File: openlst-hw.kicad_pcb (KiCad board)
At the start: 4 copper layers, 60 x 50 mm, 175 parts, among them J1 5VDC, J2 CC Prog/Debug, J3 UART0, J4 UART1, J5 Control Outputs, J6 ANT, U1 LM1117-3.3, U2 CC1110, U3 LT1086-3.6, U4 FOX924 27MHz, U5 TLV803S, U6 PE4259, U8 STA1120A, U9 RFFM6403

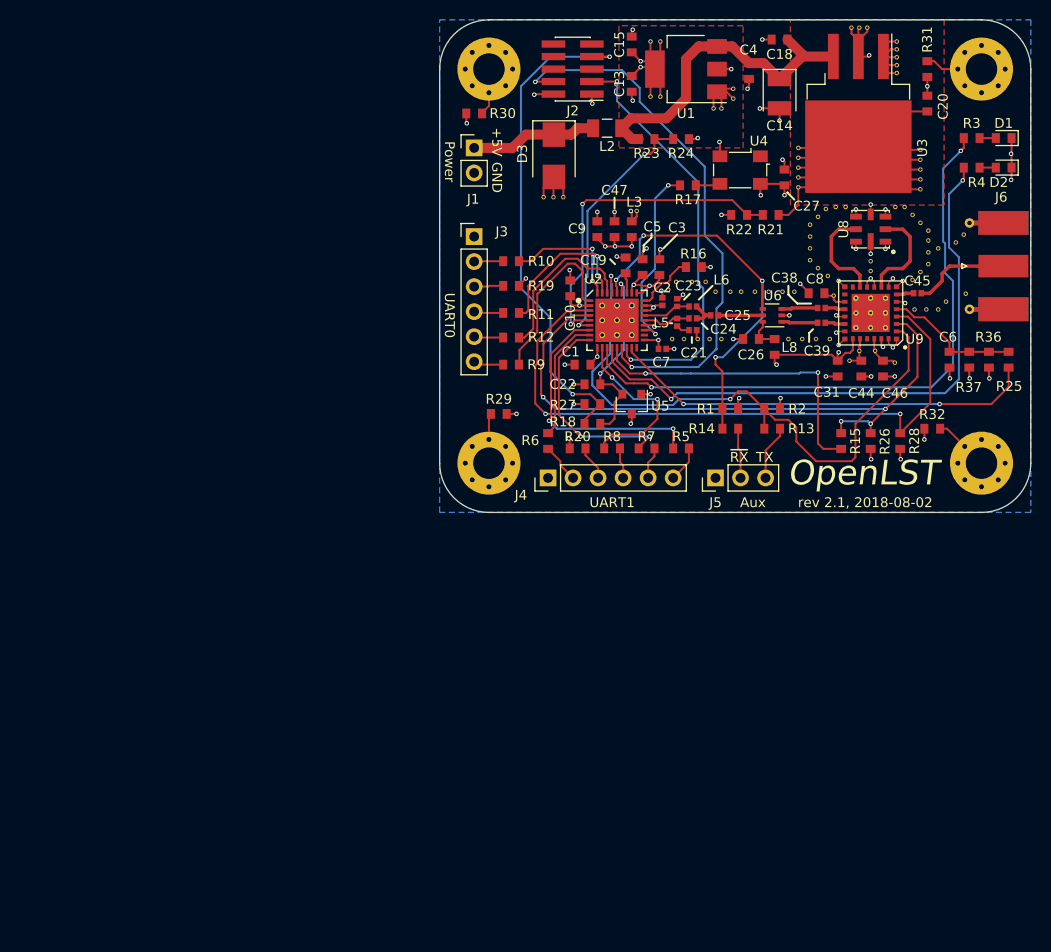
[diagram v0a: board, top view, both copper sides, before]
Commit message: Radio board done, except for artwork touchup
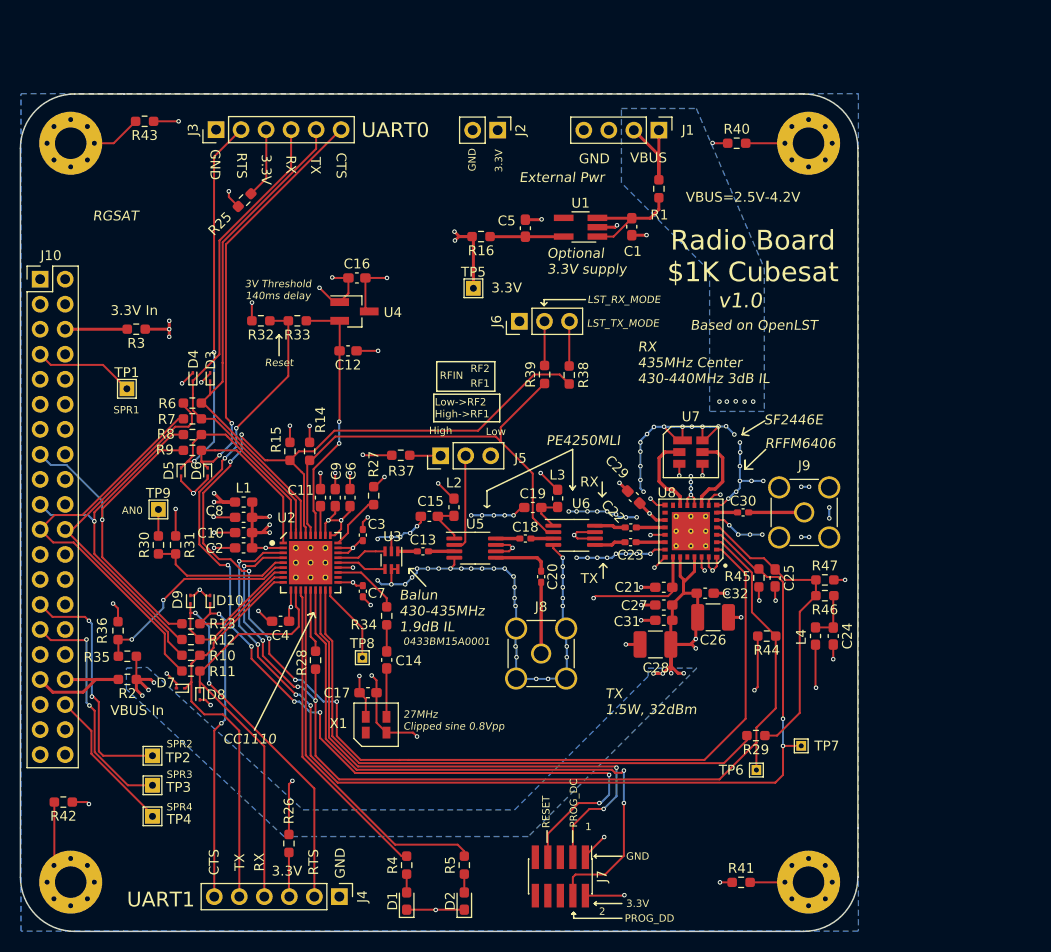
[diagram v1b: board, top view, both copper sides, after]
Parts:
- removed C38, C39, C45: 220p, archive:C_0402_1005Metric
- removed C44, C46, C47: 1u, archive:C_0603_1608Metric
- removed L5, L6: 27n, archive:L_0402_1005Metric
- removed L8: Z=1k @ 100M, archive:L_0603_1608Metric
- removed MK1, MK2, MK3, MK4: M3_Hole, archive:MountingHole_3.2mm_M3_Pad_Via
- removed R17: 100, archive:R_0603_1608Metric
- removed R18: 1K, archive:R_0603_1608Metric
- removed R19, R20: DNI, archive:R_0603_1608Metric
- removed R21, R23: 33K, archive:R_0603_1608Metric
- removed R22, R24: 10K, archive:R_0603_1608Metric
- removed REF** (x85): VIA-10mil, openlst:VIA-10mil
- removed U9: RFFM6403, openlst:Qorvo_LGA_28_ThermalVias
- added C11: 1uF, Capacitor_SMD:C_0603_1608Metric_Pad1.08x0.95mm_HandSolder, F.Cu at (101.4, 87.0)
- added C12: 0.01uF, Capacitor_SMD:C_0603_1608Metric_Pad1.08x0.95mm_HandSolder, F.Cu at (104.2, 72.1)
- added C16: 0.1uF, Capacitor_SMD:C_0603_1608Metric_Pad1.08x0.95mm_HandSolder, F.Cu at (105.1, 64.7)
- added C17: 0.1uF, Capacitor_SMD:C_0603_1608Metric_Pad1.08x0.95mm_HandSolder, F.Cu at (106.2, 106.8)
- added C28: 47uF, Capacitor_SMD:C_1210_3225Metric_Pad1.33x2.70mm_HandSolder, F.Cu at (135.4, 101.9)
- added C29: 0.1uF, Capacitor_SMD:C_0603_1608Metric_Pad1.08x0.95mm_HandSolder, F.Cu at (133.2, 87.0)
- added C30: 220pF, Capacitor_SMD:C_0402_1005Metric_Pad0.74x0.62mm_HandSolder, F.Cu at (144.3, 88.5)
- added C32: 0.1uF, Capacitor_SMD:C_0603_1608Metric_Pad1.08x0.95mm_HandSolder, F.Cu at (140.4, 96.7)
- added D10: ESD9B5.0ST5G, Diode_SMD:D_SOD-923, F.Cu at (90.2, 97.3)
- added D4: ESD9B5.0ST5G, Diode_SMD:D_SOD-923, F.Cu at (88.5, 74.8)
- added D5: ESD9B5.0ST5G, Diode_SMD:D_SOD-923, F.Cu at (87.2, 84.4)
- added D6: ESD9B5.0ST5G, Diode_SMD:D_SOD-923, F.Cu at (90.0, 84.4)
- added D7: ESD9B5.0ST5G, Diode_SMD:D_SOD-923, F.Cu at (87.2, 106.3)
- added D8: ESD9B5.0ST5G, Diode_SMD:D_SOD-923, F.Cu at (89.2, 107.1)
- added D9: ESD9B5.0ST5G, Diode_SMD:D_SOD-923, F.Cu at (88.2, 97.3)
- added H1: MountingHole_Pad, MountingHole:MountingHole_3.2mm_M3_Pad_Via, F.Cu at (150.9, 51.0)
- added H2: MountingHole_Pad, MountingHole:MountingHole_3.2mm_M3_Pad_Via, F.Cu at (150.9, 126.0)
- added H3: MountingHole_Pad, MountingHole:MountingHole_3.2mm_M3_Pad_Via, F.Cu at (76.0, 126.0)
- added H4: MountingHole_Pad, MountingHole:MountingHole_3.2mm_M3_Pad_Via, F.Cu at (76.0, 51.0)
- added J10: Conn_02x20_Odd_Even, Connector_PinHeader_2.54mm:PinHeader_2x20_P2.54mm_Vertical, F.Cu at (72.9, 64.8)
- added J7: CC Prog/Debug, Connector_PinHeader_1.27mm:PinHeader_2x05_P1.27mm_Vertical_SMD, F.Cu at (125.8, 125.5)
- added J8: Conn_Coaxial, Connector_Coaxial:SMA_Amphenol_901-144_Vertical, F.Cu at (123.8, 102.8)
- added J9: ANT, Connector_Coaxial:SMA_Amphenol_901-144_Vertical, F.Cu at (150.5, 88.5)
- added L1: Z=1k @ 100M, Inductor_SMD:L_0603_1608Metric_Pad1.05x0.95mm_HandSolder, F.Cu at (93.6, 87.5)
- added L4: Z=1k @ 100M, Inductor_SMD:L_0603_1608Metric_Pad1.05x0.95mm_HandSolder, F.Cu at (151.7, 101.0)
- added R33: 1K, Resistor_SMD:R_0603_1608Metric_Pad0.98x0.95mm_HandSolder, F.Cu at (99.0, 69.0)
- added R34: 0, Resistor_SMD:R_0603_1608Metric_Pad0.98x0.95mm_HandSolder, F.Cu at (108.1, 99.0)
- added R35: 20K, Resistor_SMD:R_0603_1608Metric_Pad0.98x0.95mm_HandSolder, F.Cu at (81.8, 103.1)
- added R38: 100, Resistor_SMD:R_0603_1608Metric_Pad0.98x0.95mm_HandSolder, F.Cu at (126.7, 74.5)
- added R39: 100, Resistor_SMD:R_0603_1608Metric_Pad0.98x0.95mm_HandSolder, F.Cu at (124.2, 74.5)
- added R40: DNP, Resistor_SMD:R_0603_1608Metric_Pad0.98x0.95mm_HandSolder, F.Cu at (143.7, 51.0)
- added R41: DNP, Resistor_SMD:R_0603_1608Metric_Pad0.98x0.95mm_HandSolder, F.Cu at (144.1, 126.0)
- added R42: DNP, Resistor_SMD:R_0603_1608Metric_Pad0.98x0.95mm_HandSolder, F.Cu at (75.3, 117.9)
- added R43: DNP, Resistor_SMD:R_0603_1608Metric_Pad0.98x0.95mm_HandSolder, F.Cu at (83.5, 48.8)
- added R44: 1K, Resistor_SMD:R_0603_1608Metric_Pad0.98x0.95mm_HandSolder, F.Cu at (146.7, 101.0)
- added R45: 1K, Resistor_SMD:R_0603_1608Metric_Pad0.98x0.95mm_HandSolder, F.Cu at (145.9, 95.2)
- added R46: 3.09K, Resistor_SMD:R_0603_1608Metric_Pad0.98x0.95mm_HandSolder, F.Cu at (152.6, 97.0)
- added R47: 6.65K, Resistor_SMD:R_0603_1608Metric_Pad0.98x0.95mm_HandSolder, F.Cu at (152.6, 95.3)
- added TP1: TP_1.5x1.5, TestPoint:TestPoint_THTPad_1.5x1.5mm_Drill0.7mm, F.Cu at (81.8, 76.0)
- added TP2: TP_1.5x1.5, TestPoint:TestPoint_THTPad_1.5x1.5mm_Drill0.7mm, F.Cu at (84.3, 113.2)
- added TP3: TP_1.5x1.5, TestPoint:TestPoint_THTPad_1.5x1.5mm_Drill0.7mm, F.Cu at (84.3, 116.2)
- added TP4: TP_1.5x1.5, TestPoint:TestPoint_THTPad_1.5x1.5mm_Drill0.7mm, F.Cu at (84.3, 119.3)
- added TP5: TP_1.5x1.5, TestPoint:TestPoint_THTPad_1.5x1.5mm_Drill0.7mm, F.Cu at (116.9, 65.8)
- added TP6: TP_tht_1x1, TestPoint:TestPoint_THTPad_1.0x1.0mm_Drill0.5mm, F.Cu at (145.7, 114.7)
- added TP7: TP_tht_1x1, TestPoint:TestPoint_THTPad_1.0x1.0mm_Drill0.5mm, F.Cu at (150.2, 112.2)
- added TP8: TP_tht_1x1, TestPoint:TestPoint_THTPad_1.0x1.0mm_Drill0.5mm, F.Cu at (105.7, 103.2)
- added TP9: TP_1.5x1.5, TestPoint:TestPoint_THTPad_1.5x1.5mm_Drill0.7mm, F.Cu at (85.0, 88.2)
- added U7: SF2446E, footprint_custom:SF2446E, F.Cu at (139.0, 82.4)
- added X1: TG2520SMN 27MHz, footprint_custom:TG2520SMN, F.Cu at (107.0, 110.0)
- C1, C31, C5: value 0.1u -> 4.7uF; footprint archive:C_0603_1608Metric -> Capacitor_SMD:C_0603_1608Metric_Pad1.08x0.95mm_HandSolder
- C10, C27, C8: value 0.1u -> 1uF; footprint archive:C_0603_1608Metric -> Capacitor_SMD:C_0603_1608Metric_Pad1.08x0.95mm_HandSolder
- C13, C18, C20: value 10u -> 220pF; footprint archive:C_0603_1608Metric -> Capacitor_SMD:C_0402_1005Metric_Pad0.74x0.62mm_HandSolder
- C14: value 100u -> 0.01uF; footprint archive:CP_EIA-3528-15_AVX-H -> Capacitor_SMD:C_0603_1608Metric_Pad1.08x0.95mm_HandSolder
- C15, C6: value 0.1u -> 0.1uF; footprint archive:C_0603_1608Metric -> Capacitor_SMD:C_0603_1608Metric_Pad1.08x0.95mm_HandSolder
- C19: value 1n -> 0.1uF; footprint archive:C_0603_1608Metric -> Capacitor_SMD:C_0603_1608Metric_Pad1.08x0.95mm_HandSolder
- C2, C21, C25: value 220p -> 0.1uF; footprint archive:C_0402_1005Metric -> Capacitor_SMD:C_0603_1608Metric_Pad1.08x0.95mm_HandSolder
- C22: value 1n -> 220pF; footprint archive:C_0603_1608Metric -> Capacitor_SMD:C_0402_1005Metric_Pad0.74x0.62mm_HandSolder
- C23: value 3.9p -> 220pF; footprint archive:C_0402_1005Metric -> Capacitor_SMD:C_0402_1005Metric_Pad0.74x0.62mm_HandSolder
- C24: value 3.9p -> 0.1uF; footprint archive:C_0402_1005Metric -> Capacitor_SMD:C_0603_1608Metric_Pad1.08x0.95mm_HandSolder
- C26: value 0.1u -> 47uF; footprint archive:C_0603_1608Metric -> Capacitor_SMD:C_1210_3225Metric_Pad1.33x2.70mm_HandSolder
- C3: value 0.1u -> 220pF; footprint archive:C_0603_1608Metric -> Capacitor_SMD:C_0402_1005Metric_Pad0.74x0.62mm_HandSolder
- C4: value 10u -> 0.1uF; footprint archive:C_0603_1608Metric -> Capacitor_SMD:C_0603_1608Metric_Pad1.08x0.95mm_HandSolder
- C7: value 220p -> 220pF; footprint archive:C_0402_1005Metric -> Capacitor_SMD:C_0402_1005Metric_Pad0.74x0.62mm_HandSolder
- C9: value 1u -> 0.1uF; footprint archive:C_0603_1608Metric -> Capacitor_SMD:C_0603_1608Metric_Pad1.08x0.95mm_HandSolder
- D1, D2: value LED -> LED_SMD_RED; footprint archive:LED_0603_1608Metric -> LED_SMD:LED_0603_1608Metric_Pad1.05x0.95mm_HandSolder
- D3: value STPS340U -> ESD9B5.0ST5G; footprint archive:D_SMB -> Diode_SMD:D_SOD-923
- J1: value 5VDC -> EXT VBUS; footprint archive:PinHeader_1x02_P2.54mm_Vertical -> Connector_PinHeader_2.54mm:PinHeader_1x04_P2.54mm_Vertical
- J2: value CC Prog/Debug -> EXT 3.3V; footprint archive:PinHeader_2x05_P1.27mm_Vertical_SMD -> Connector_PinHeader_2.54mm:PinHeader_1x02_P2.54mm_Vertical
- J3, J4: footprint archive:PinHeader_1x06_P2.54mm_Vertical -> Connector_PinHeader_2.54mm:PinHeader_1x06_P2.54mm_Vertical
- J5: value Control Outputs -> Switch Select; footprint archive:PinHeader_1x03_P2.54mm_Vertical -> Connector_PinHeader_2.54mm:PinHeader_1x03_P2.54mm_Vertical
- J6: value ANT -> Control Outputs; footprint archive:SMA_Molex_73251-1153_EdgeMount_Horizontal -> Connector_PinHeader_2.54mm:PinHeader_1x03_P2.54mm_Vertical
- L2: value Z=500 @ 100M -> Z=1k @ 100M; footprint archive:L_1206_3216Metric -> Inductor_SMD:L_0603_1608Metric_Pad1.05x0.95mm_HandSolder
- L3: footprint archive:L_0603_1608Metric -> Inductor_SMD:L_0603_1608Metric_Pad1.05x0.95mm_HandSolder
- R1, R26, R28: value 1K -> DNP; footprint archive:R_0603_1608Metric -> Resistor_SMD:R_0603_1608Metric_Pad0.98x0.95mm_HandSolder
- R10, R11, R12, R13: value 100 -> DNP; footprint archive:R_0603_1608Metric -> Resistor_SMD:R_0603_1608Metric_Pad0.98x0.95mm_HandSolder
- R14, R5: value 100 -> 1K; footprint archive:R_0603_1608Metric -> Resistor_SMD:R_0603_1608Metric_Pad0.98x0.95mm_HandSolder
- R15: value DNI -> 1K; footprint archive:R_0603_1608Metric -> Resistor_SMD:R_0603_1608Metric_Pad0.98x0.95mm_HandSolder
- R16: value 56K -> 0; footprint archive:R_0603_1608Metric -> Resistor_SMD:R_0603_1608Metric_Pad0.98x0.95mm_HandSolder
- R2, R3: value 1K -> 10m; footprint archive:R_0603_1608Metric -> Resistor_SMD:R_0603_1608Metric_Pad0.98x0.95mm_HandSolder
- R25, R29, R30, R31: value DNI -> DNP; footprint archive:R_0603_1608Metric -> Resistor_SMD:R_0603_1608Metric_Pad0.98x0.95mm_HandSolder
- R27: value 33K -> 56K; footprint archive:R_0603_1608Metric -> Resistor_SMD:R_0603_1608Metric_Pad0.98x0.95mm_HandSolder
- R32: value DNI -> 47K; footprint archive:R_0603_1608Metric -> Resistor_SMD:R_0603_1608Metric_Pad0.98x0.95mm_HandSolder
- R36: value 5K6 -> 47K; footprint archive:R_0603_1608Metric -> Resistor_SMD:R_0603_1608Metric_Pad0.98x0.95mm_HandSolder
- R37: value 3K3 -> 1K; footprint archive:R_0603_1608Metric -> Resistor_SMD:R_0603_1608Metric_Pad0.98x0.95mm_HandSolder
- R4, R6, R7, R8, R9: footprint archive:R_0603_1608Metric -> Resistor_SMD:R_0603_1608Metric_Pad0.98x0.95mm_HandSolder
- U1: value LM1117-3.3 -> ADP150AUJZ-3.3-R7; footprint archive:SOT-223-3_TabPin2 -> Package_TO_SOT_SMD:TSOT-23-5_HandSoldering
- U3: value LT1086-3.6 -> 0433BM15A0001; footprint archive:TO-263-3_TabPin2 -> RF_Converter:Balun_Johanson_0896BM15A0001
- U4: value FOX924 27MHz -> MIC803; footprint archive:Oscillator_SMD_Fordahl_DFAS15-4Pin_5.0x3.2mm -> Package_TO_SOT_SMD:SOT-23_Handsoldering
- U5: value TLV803S -> PE4250MLI; footprint archive:SOT-23 -> Package_SO:MSOP-8_3x3mm_P0.65mm
- U6: value PE4259 -> PE4250MLI; footprint archive:SOT-363_SC-70-6 -> Package_SO:MSOP-8_3x3mm_P0.65mm
- U8: value STA1120A -> RFFM6406; footprint openlst:SAW-8_3.8mm -> openlst:Qorvo_LGA_28_ThermalVias
- moved D1 98.3 mm to (110.2, 128.0), turned to 90 degrees
- moved R36 92.6 mm to (80.8, 100.5)
- moved D2 92.4 mm to (116.0, 128.0), turned to 90 degrees
- moved R4 91.1 mm to (110.2, 124.3), turned to 90 degrees
- moved R31 90.3 mm to (86.7, 91.8), turned to 270 degrees
- moved R3 87.0 mm to (82.7, 69.9)
- moved R25 79.2 mm to (93.7, 56.8), turned to 225 degrees
- moved C4 73.4 mm to (97.3, 99.5), turned to 180 degrees
- moved R26 71.8 mm to (98.2, 122.1)
- moved R2 71.0 mm to (81.8, 105.5)
- moved C14 70.0 mm to (108.1, 103.5), turned to 90 degrees
- moved R32 69.0 mm to (95.3, 69.0), turned to 180 degrees
- moved U3 65.6 mm to (108.6, 93.3)
- moved R28 63.4 mm to (100.9, 103.5)
- moved C8 62.4 mm to (93.6, 89.0)
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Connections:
- C1 pad 1: /3V3_FILT -> Net-(C1-Pad1)
- C13 pad 1: +3V3 -> Net-(C13-Pad1)
- C13 pad 2: GND -> Net-(C13-Pad2)
- C14 pad 1: +5V -> Net-(C14-Pad1)
- C14 pad 2: GND -> Net-(C14-Pad2)
- C15 pad 1: +3V3 -> Net-(C15-Pad1)
- C18 pad 1: +5V -> Net-(C18-Pad1)
- C18 pad 2: GND -> Net-(C18-Pad2)
- C20 pad 1: VCC_3V6 -> Net-(C20-Pad1)
- C20 pad 2: GND -> Net-(C20-Pad2)
- C21 pad 1: GND -> +3V3
- C21 pad 2: Net-(C21-Pad2) -> GND
- C22 pad 2: GND -> Net-(C22-Pad2)
- C23 pad 1: GND -> Net-(C23-Pad1)
- C24 pad 2: Net-(C24-Pad2) -> GND
- C25 pad 1: Net-(C24-Pad2) -> /PA_VAPC
- C25 pad 2: Net-(C25-Pad2) -> GND
- C26 pad 1: Net-(C26-Pad1) -> VBUS
- C27 pad 1: +3V3 -> VBUS
- C31 pad 1: +3V3 -> VBUS
- C4 pad 1: +5V -> /3V3_FILT
- C5 pad 1: /3V3_FILT -> Net-(C5-Pad1)
- C6 pad 1: /PA_VAPC -> /3V3_FILT
- C8 pad 1: VCC_3V6 -> /3V3_FILT
- C9 pad 1: GND -> /3V3_FILT
- C9 pad 2: /3V3_FILT -> GND
- D3 pad 1: Net-(D3-Pad1) -> /UART0_TX
- J1 pad 1: Net-(D3-Pad1) -> VBUS
- J1 pad 2: GND -> VBUS
- J2 pad 1: GND -> +3V3
- J2 pad 2: +3V3 -> GND
- J5 pad 1: GND -> Net-(J5-Pad1)
- J5 pad 3: Net-(J5-Pad3) -> GND
- J6 pad 1: Net-(C45-Pad1) -> GND
- J6 pad 2: GND -> Net-(J6-Pad2)
- L2 pad 1: +5V -> Net-(C15-Pad1)
- L2 pad 2: Net-(D3-Pad1) -> +3V3
- L3 pad 1: +3V3 -> Net-(C19-Pad1)
- L3 pad 2: /3V3_FILT -> +3V3
- R1 pad 1: +3V3 -> Net-(C1-Pad1)
- R1 pad 2: /~LST_RX_MODE -> VBUS
- R10 pad 1: Net-(R10-Pad1) -> /INTERBOARD_CONNECTOR2/UART_B_RXI
- R10 pad 2: /UART0_RTS -> /UART1_TX
- R11 pad 1: Net-(R11-Pad1) -> /INTERBOARD_CONNECTOR2/UART_B_TXO
- R11 pad 2: /UART0_RX -> /UART1_RX
- R12 pad 1: Net-(R12-Pad1) -> /INTERBOARD_CONNECTOR2/UART_B_CTS
- R12 pad 2: /UART0_TX -> /UART1_RTS
- R13 pad 1: /LST_TX_MODE -> /INTERBOARD_CONNECTOR2/UART_B_RTS
- R13 pad 2: Net-(J5-Pad3) -> /UART1_CTS
- R14 pad 2: Net-(J5-Pad2) -> +3V3
- R15 pad 1: /RF_EN -> GND
- R15 pad 2: Net-(R15-Pad2) -> /LST_TX_MODE
- R16 pad 1: GND -> Net-(C5-Pad1)
- R16 pad 2: Net-(R16-Pad2) -> +3V3
- R2 pad 1: GND -> VBUS
- R2 pad 2: /LST_TX_MODE -> /INTERBOARD_CONNECTOR2/5V0_2
- R25 pad 1: /PA_VAPC -> Net-(J3-Pad3)
- R25 pad 2: Net-(R25-Pad2) -> +3V3
- R26 pad 1: +3V3 -> Net-(J4-Pad3)
- R26 pad 2: /RF_EN -> +3V3
- R27 pad 1: /~LST_RESET -> Net-(R27-Pad1)
- R27 pad 2: +3V3 -> GND
- R28 pad 1: /RF_BYP -> Net-(R28-Pad1)
- R28 pad 2: GND -> /RF_EN
- R29 pad 1: GND -> /PA_VAPC
- R29 pad 2: Net-(MK1-Pad1) -> Net-(R29-Pad2)
- R3 pad 1: Net-(D1-Pad2) -> +3V3
- R3 pad 2: Net-(R3-Pad2) -> /INTERBOARD_CONNECTOR2/3V3_10
- R30 pad 1: GND -> /AN0
- R31 pad 2: Net-(MK3-Pad1) -> /AN0
- R32 pad 1: GND -> /~LST_RESET
- R32 pad 2: Net-(MK4-Pad1) -> +3V3
- R36 pad 1: /PA_VAPC -> GND
- R36 pad 2: GND -> /AN1
- R37 pad 1: VCC_3V6 -> +3V3
- R37 pad 2: /PA_VAPC -> Net-(J5-Pad1)
- R4 pad 1: Net-(D2-Pad2) -> Net-(D1-Pad2)
- R5 pad 1: Net-(R5-Pad1) -> Net-(D2-Pad2)
- R5 pad 2: /UART1_CTS -> Net-(R5-Pad2)
- R6 pad 1: Net-(R6-Pad1) -> /UART0_TX
- R6 pad 2: /UART1_RTS -> /INTERBOARD_CONNECTOR2/UART_B_RXI
- R7 pad 1: Net-(R7-Pad1) -> /UART0_RX
- R7 pad 2: /UART1_TX -> /INTERBOARD_CONNECTOR2/UART_B_TXO
- R8 pad 1: Net-(R8-Pad1) -> /UART0_RTS
- R8 pad 2: /UART1_RX -> /INTERBOARD_CONNECTOR2/UART_B_CTS
- R9 pad 1: Net-(R9-Pad1) -> /UART0_CTS
- R9 pad 2: /UART0_CTS -> /INTERBOARD_CONNECTOR2/UART_B_RTS
- U1 pad 1: GND -> Net-(C1-Pad1)
- U1 pad 2: +3V3 -> GND
- U1 pad 3: +5V -> Net-(C1-Pad1)
- U2 pad 1: Net-(R9-Pad1) -> /UART0_CTS
- U2 pad 11: Net-(R8-Pad1) -> /UART1_RX
- U2 pad 12: Net-(R3-Pad2) -> Net-(R4-Pad2)
- U2 pad 13: Net-(R4-Pad2) -> Net-(R5-Pad2)
- U2 pad 14: Net-(R15-Pad2) -> Net-(R28-Pad1)
- U2 pad 17: Net-(R25-Pad2) -> Net-(R29-Pad2)
- U2 pad 20: Net-(U2-Pad20) -> (no net)
- U2 pad 23: Net-(C24-Pad1) -> Net-(U2-Pad23)
- U2 pad 24: Net-(C23-Pad2) -> Net-(U2-Pad24)
- U2 pad 27: Net-(R16-Pad2) -> Net-(R27-Pad1)
- U2 pad 30: Net-(C19-Pad1) -> Net-(C11-Pad1)
- U2 pad 31: Net-(C22-Pad1) -> Net-(C12-Pad2)
- U2 pad 34: Net-(R12-Pad1) -> /UART0_TX
- U2 pad 35: Net-(R11-Pad1) -> /UART0_RX
- U2 pad 36: Net-(R10-Pad1) -> /UART0_RTS
- U2 pad 7: Net-(R5-Pad1) -> /UART1_CTS
- U2 pad 8: Net-(R6-Pad1) -> /UART1_RTS
- U2 pad 9: Net-(R7-Pad1) -> /UART1_TX
- U3 pad 1: GND -> Net-(C13-Pad1)
- U3 pad 2: VCC_3V6 -> GND
- U3 pad 3: +5V -> Net-(U2-Pad24)
- U4 pad 1: (no net) -> GND
- U4 pad 2: GND -> Net-(C12-Pad2)
- U4 pad 3: Net-(R17-Pad1) -> +3V3
- U5 pad 1: GND -> Net-(C15-Pad1)
- U5 pad 2: Net-(C22-Pad1) -> Net-(J5-Pad2)
- U5 pad 3: +3V3 -> Net-(C13-Pad2)
- U6 pad 1: Net-(C39-Pad1) -> Net-(C19-Pad1)
- U6 pad 2: GND -> /~LST_RX_MODE
- U6 pad 3: Net-(C38-Pad1) -> Net-(C18-Pad2)
- U6 pad 4: /~LST_RX_MODE -> GND
- U6 pad 5: Net-(C25-Pad2) -> Net-(C23-Pad1)
- U6 pad 6: Net-(C26-Pad1) -> GND
- U8 pad 2: Net-(U8-Pad2) -> /LST_TX_MODE
- U8 pad 3: GND -> /RF_EN
- U8 pad 4: GND -> /RF_BYP
- U8 pad 5: GND -> /PA_VAPC
- U8 pad 6: Net-(U8-Pad6) -> GND
- U8 pad 7: GND -> Net-(C30-Pad1)
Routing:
- net GND: track 94.4 -> 239.9 mm, vias 56 -> 146
- net VCC_3V6: track 105.7 -> 0.00 mm, vias 2 -> 0
- net /LST_TX_MODE: track 63.9 -> 149.7 mm, vias 2 -> 6
- net Net-(R3-Pad2): track 63.1 -> 0.00 mm, vias 2 -> 0
- net Net-(R29-Pad2): track 0.00 -> 59.8 mm
- net VBUS: track 0.00 -> 58.2 mm, vias 0 -> 15
- net /UART0_CTS: track 3.07 -> 57.8 mm, vias 0 -> 2
- net /UART0_RTS: track 2.97 -> 56.0 mm, vias 0 -> 2
- net /UART0_TX: track 2.99 -> 51.6 mm
- net /UART0_RX: track 3.00 -> 50.4 mm
- net /~LST_RESET: track 51.4 -> 97.5 mm, vias 2 -> 8
- net /UART1_RTS: track 4.00 -> 49.4 mm, vias 0 -> 2
- net Net-(R25-Pad2): track 43.6 -> 0.00 mm, vias 2 -> 0
- net /INTERBOARD_CONNECTOR2/UART_B_TXO: track 0.00 -> 40.7 mm
- net /RF_BYP: track 67.7 -> 107.4 mm, vias 2 -> 6
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- added copper zone on B.Cu, net VBUS
- added copper zone on In2.Cu, net VBUS
- removed copper zone on F.Cu, net +3V3
- removed copper zone on F.Cu, net VCC_3V6
- removed copper zone on In2.Cu, net VCC_3V6
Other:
- board size 60 x 50 mm -> 85 x 85 mm
- net class 50ohm: trace_width 0.35052 -> 0.345
- board text added: "0433BM15A0001"
- board text added: "1"
- board text added: "2"
- board text added: "27MHz Clipped sine 0.8Vpp"
- board text added: "3.3V"
- board text added: "3.3V In"
- board text added: "3V Threshold 140ms delay"
- board text added: "AN0"
- board text added: "Balun 430-435MHz 1.9dB IL"
- board text added: "Based on OpenLST"
- board text added: "CC1110"
- board text added: "CTS"
- board text added: "External Pwr"
- board text added: "High"
- board text added: "LST_RX_MODE"
- board text added: "LST_TX_MODE"
- board text added: "Low"
- board text added: "Low->RF2 High->RF1"
- board text added: "Optional 3.3V supply"
- board text added: "PE4250MLI"
- board text added: "PROG_DC"
- board text added: "PROG_DD"
- board text added: "RESET"
- board text added: "RF1"
- board text added: "RF2"
- board text added: "RFFM6406"
- board text added: "RFIN"
- board text added: "RGSAT"
- board text added: "RTS"
- board text added: "RX"
- board text added: "RX 435MHz Center 430-440MHz 3dB IL"
- board text added: "Radio Board $1K Cubesat"
- board text added: "Reset"
- board text added: "SF2446E"
- board text added: "SPR1"
- board text added: "SPR2"
- board text added: "SPR3"
- board text added: "SPR4"
- board text added: "TX 1.5W, 32dBm"
- board text added: "VBUS"
- board text added: "VBUS In"
- board text added: "VBUS=2.5V-4.2V"
- board text added: "v1.0"
- board text removed: "+5V"
- board text removed: "Aux"
- board text removed: "OpenLST"
- board text removed: "Power"
- board text removed: "This work is licensed under a Creative Commons Attribution-ShareAlike 4.0 International License (CC-BY-SA 4.0)."
- board text removed: "rev 2.1, 2018-08-02"
- board text removed: "rwk"
- board text removed: "~RX"

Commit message: Final before gerbers are generated
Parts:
- added H5: MountingHole, MountingHole:MountingHole_2.7mm, F.Cu at (136.5, 119.3)
- added H6: MountingHole, MountingHole:MountingHole_2.7mm, F.Cu at (110.5, 57.1)
- added H7: MountingHole, MountingHole:MountingHole_2.7mm, F.Cu at (86.0, 63.4)
- added LOGO1: Logo_Open_Hardware_Small, footprint_custom:a1, F.Cu at (117.5, 79.2)
- added LOGO2: Logo_Open_Hardware_Small, footprint_custom:a2, F.Cu at (98.6, 102.9)
- added LOGO3: Logo_Open_Hardware_Small, Symbol:OSHW-Logo2_24.3x20mm_SilkScreen, F.Cu at (134.1, 61.3)
- renumbered J10 to J1, J1 to J10
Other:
- board text added: "Always has been"
- board text added: "RG SAT"
- board text added: "Wait, it's all open source?"
- board text added: "subscribe"
- board text removed: "RGSAT"
